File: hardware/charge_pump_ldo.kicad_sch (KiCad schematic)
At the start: 1 part, among them U5 LM27762

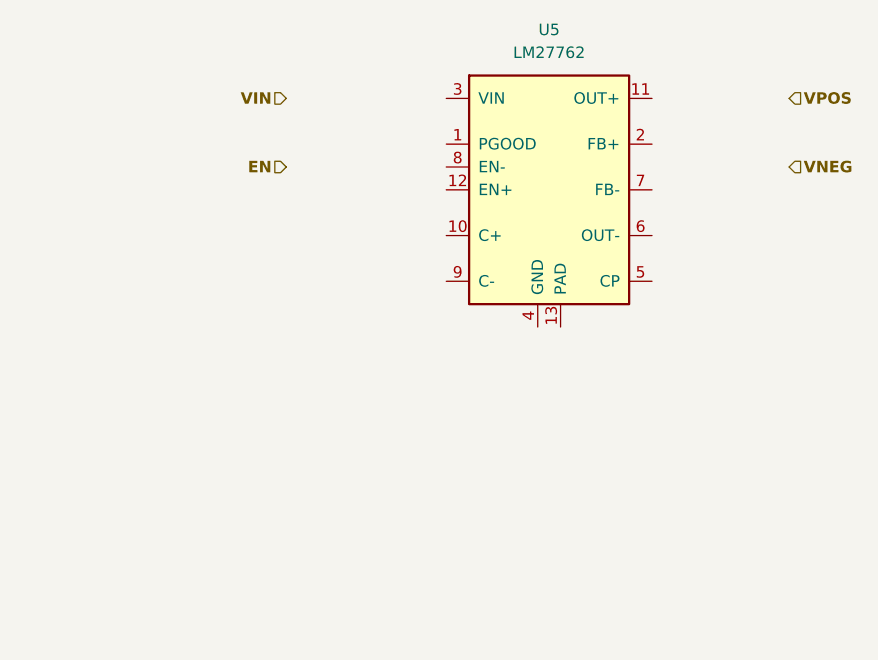
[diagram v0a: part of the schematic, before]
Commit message: Add USB sheet and remove old components
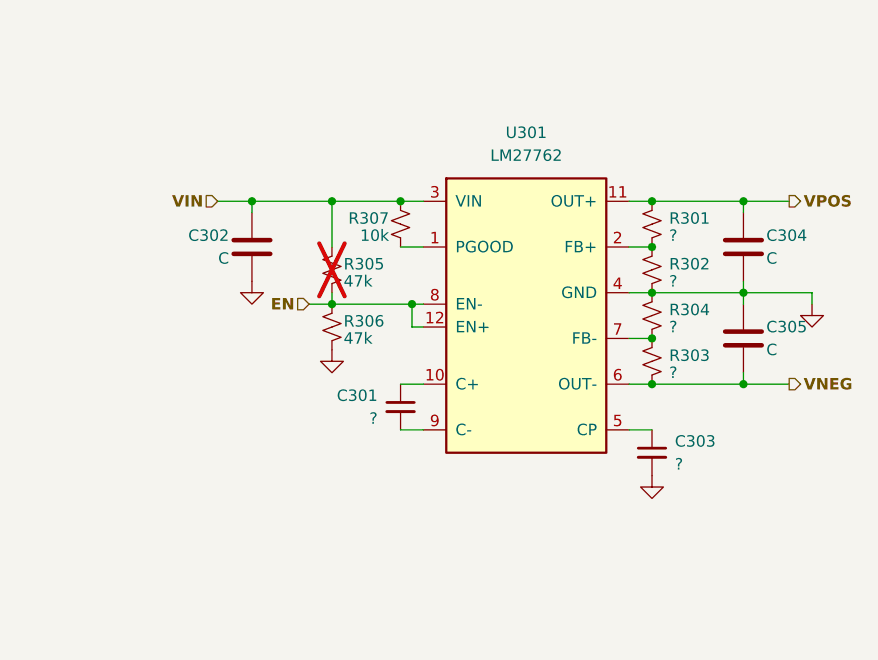
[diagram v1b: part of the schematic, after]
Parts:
- added C301, C303: ?, symbol Device:C_Small
- added C302, C304, C305: C, symbol Device:C
- added R301, R302, R303, R304: ?, symbol Device:R_Small_US
- added R305, R306: 47k, symbol Device:R_Small_US
- added R307: 10k, symbol Device:R_Small_US
- renumbered U5 to U301
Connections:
- net EN: now also U301.12 (EN+), U301.8 (EN-), R305.2, R306.1
- net VIN: now also U301.3 (VIN), C302.1, R305.1, R307.1
- net VNEG: now also U301.6 (OUT-), C305.2, R303.2
- net VPOS: now also U301.11 (OUT+), C304.1, R301.1
- net at U301.1 (PGOOD): now also R307.2
- net at U301.10 (C+): now also C301.1
- net GND: now reaches U301.13 (PAD)
- net GND: now also U301.4 (GND), C302.2, C303.2, C304.2, C305.1, R302.2, R304.1, R306.2
- net at U301.2 (FB+): now also R301.2, R302.1
- net at U301.5 (CP): now also C303.1
- net at U301.7 (FB-): now also R303.1, R304.2
- net at U301.9 (C-): now also C301.2

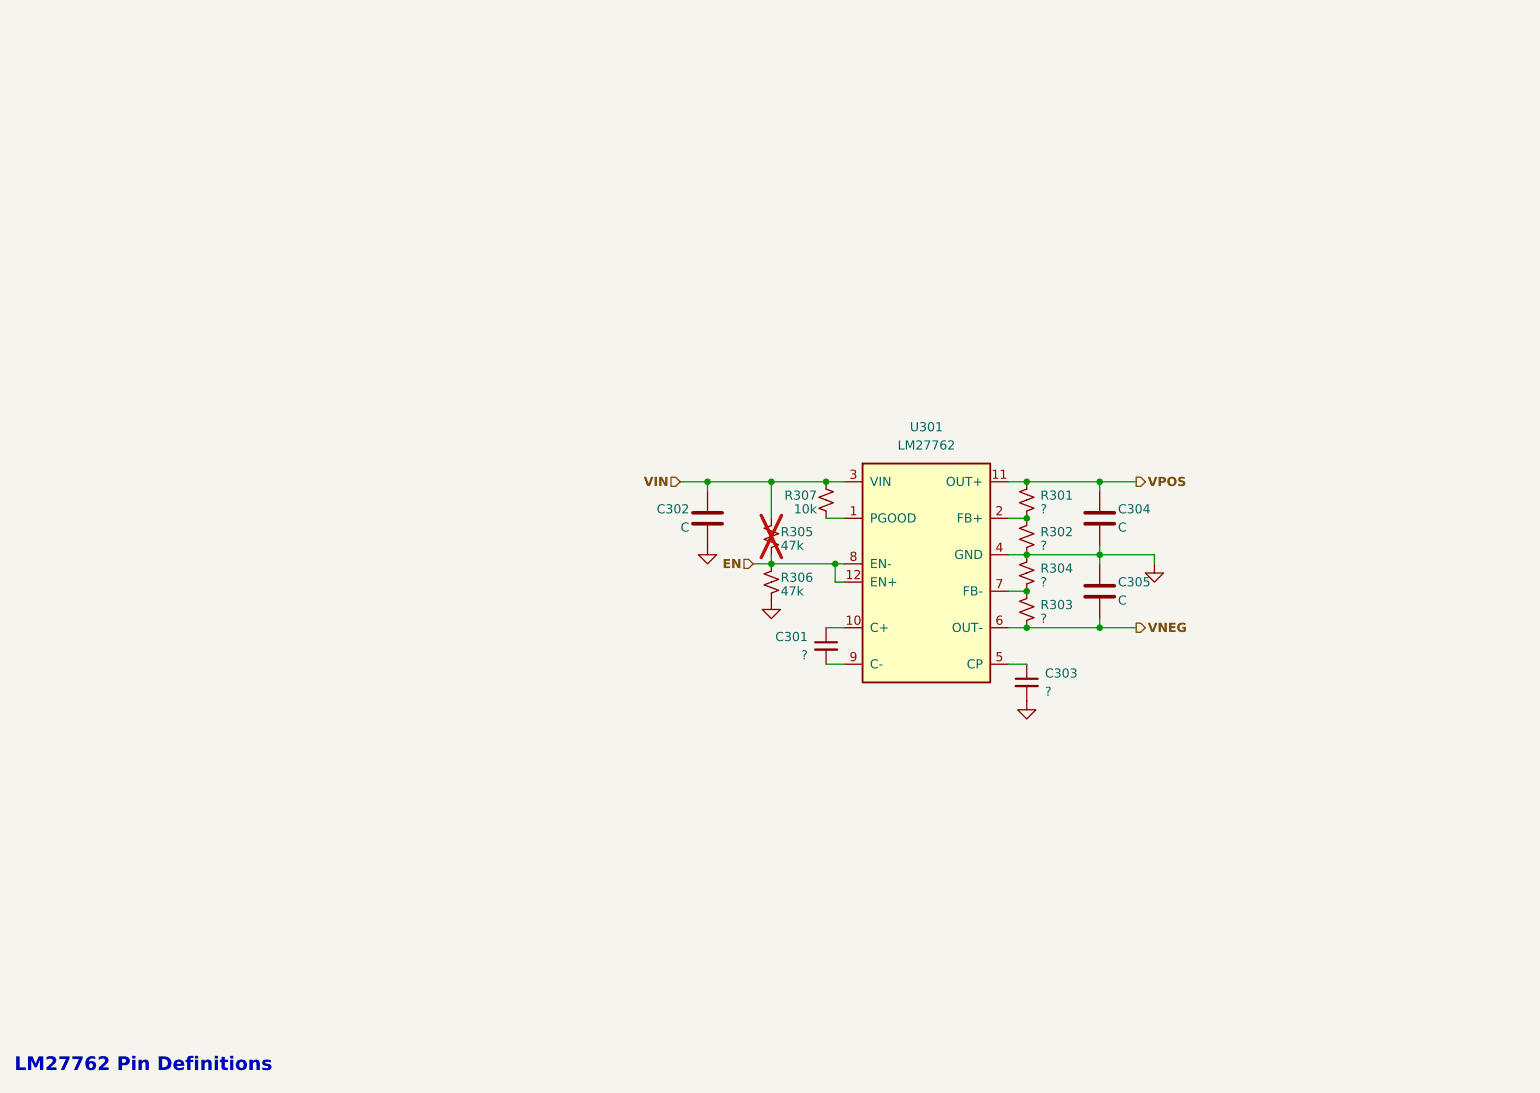
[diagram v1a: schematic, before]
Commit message: Finalize 5V rails
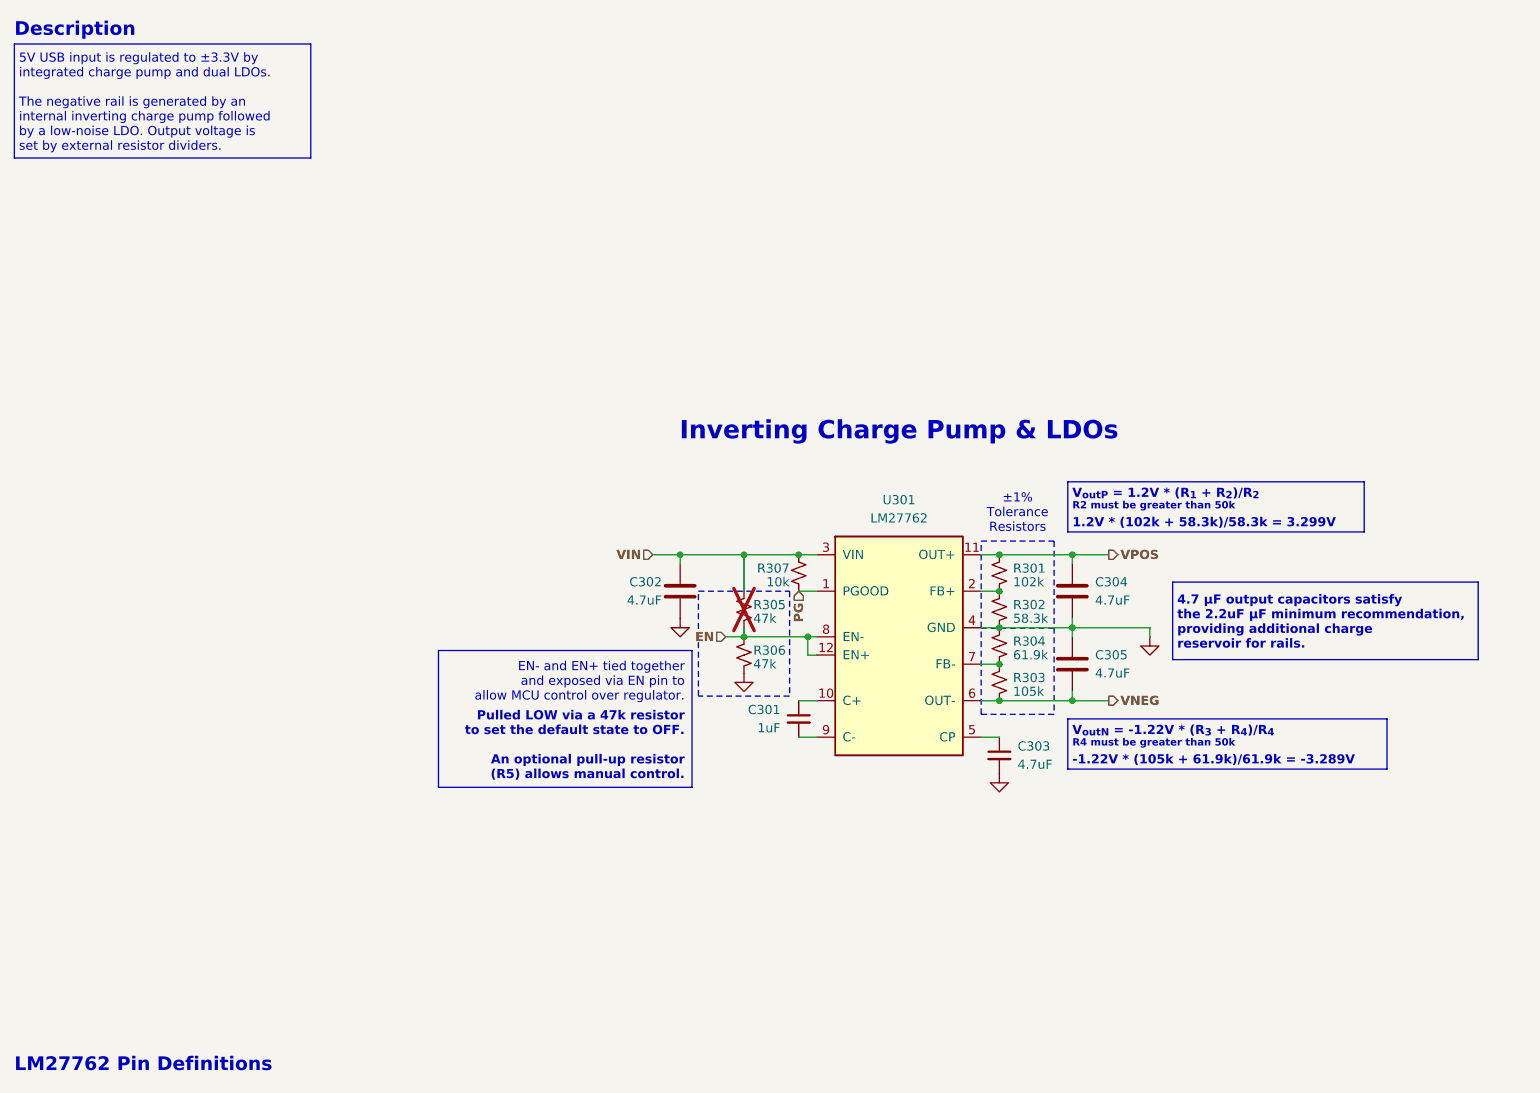
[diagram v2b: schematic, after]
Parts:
- C301: value ? -> 1uF
- C302, C304, C305: value C -> 4.7uF
- C303: value ? -> 4.7uF
- R301: value ? -> 102k; Tolerance (none) -> ±1%
- R302: value ? -> 58.3k; Tolerance (none) -> ±1%
- R303: value ? -> 105k; Tolerance (none) -> ±1%
- R304: value ? -> 61.9k; Tolerance (none) -> ±1%
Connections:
- net PG: now reaches R307.2, U301.1 (PGOOD)
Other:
- note added: "4.7 µF output capacitors satisfy the 2.2uF µF minimum recommendation, providing additional charge reservoir for rails."
- note added: "5V USB input is regulated to ±3.3V by integrated charge pump and dual LDOs. The negative rail is generated by an internal inverting charge pump followed by a low-noise LDO. Output voltage is set by external resistor dividers."
- note added: "Description"
- note added: "EN- and EN+ tied together and exposed via EN pin to allow MCU control over regulator."
- note added: "Inverting Charge Pump & LDOs"
- note added: "Pulled LOW via a 47k resistor to set the default state to OFF. An optional pull-up resistor (R5) allows manual control."
- note added: "V_{outN} = -1.22V * (R_{3} + R_{4})/R_{4} ^{R4 must be greater than 50k} -1.22V * (105k + 61.9k)/61.9k = -3.289V"
- note added: "V_{outP} = 1.2V * (R_{1} + R_{2})/R_{2} ^{R2 must be greater than 50k} 1.2V * (102k + 58.3k)/58.3k = 3.299V"
- note added: "±1% Tolerance Resistors"
- moved on the sheet: C301, C302, C303, C304, C305, R301, R302, R303, R304, R305, R306, R307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

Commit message: Finalize USB interface
Added soft-start
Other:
- title: ±5V Rail Charge Pump & Regulators -> ±3.3V Rail Charge Pump & Regulators
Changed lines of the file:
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@@
 	(paper "A")
 	(title_block
-		(title "±5V Rail Charge Pump & Regulators")
+		(title "±3.3V Rail Charge Pump & Regulators")
 		(rev "A")
 		(company "Jacob Wigent")

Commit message: Finalize power
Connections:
- net VIN renamed VBUS_SW
- net VBUS_SW: no longer R307.1
- net VNEG renamed -3.3VA
- net VPOS renamed +3.3VA
- new net +3.3VD: R307.1
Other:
- note added: "PGOOD exposed with 10k pullup to 3.3VD for MCU monitoring."
- moved on the sheet: R307

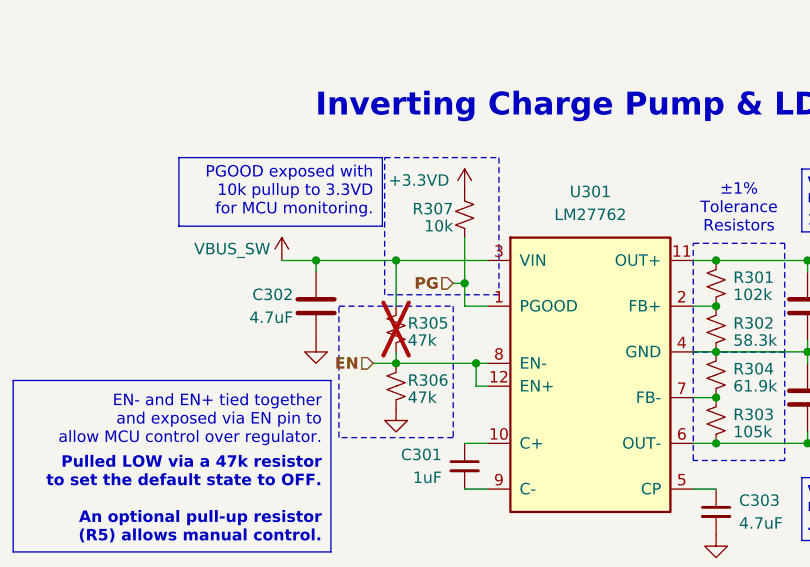
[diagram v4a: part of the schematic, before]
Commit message: Begin MCU pin assignments
Added STM32CubeMX project. Assigned peripheral pins, and began assigning GPIOs.
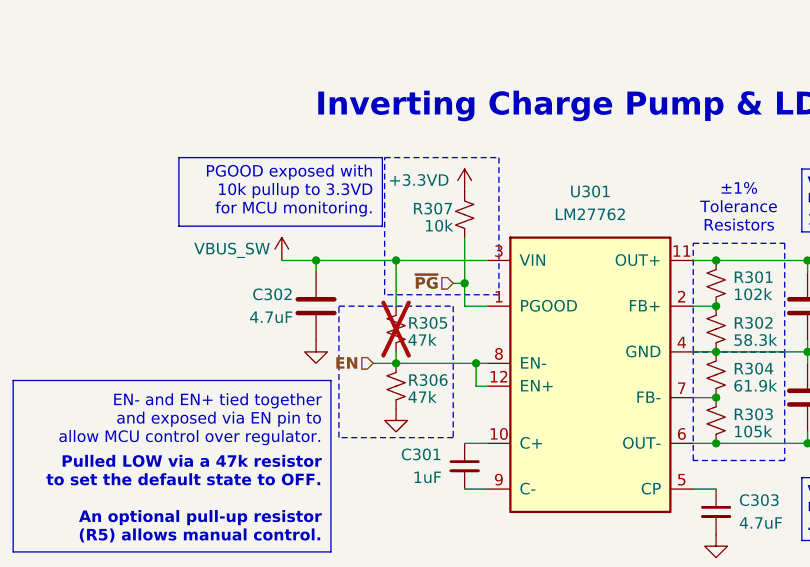
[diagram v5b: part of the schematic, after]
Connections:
- net PG renamed ~{PG}
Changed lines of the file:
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@@
 		)
 	)
-	(hierarchical_label "PG"
+	(hierarchical_label "~{PG}"
 		(shape input)
 		(at 120.65 90.17 180)

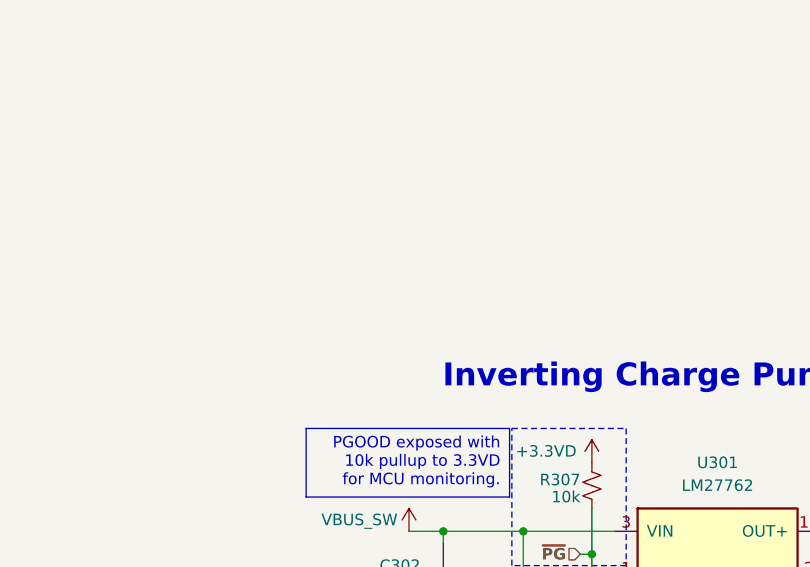
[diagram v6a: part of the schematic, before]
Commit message: Begin VGA impl
Sim and notes on adjusting to 4.5V rails for VGA.
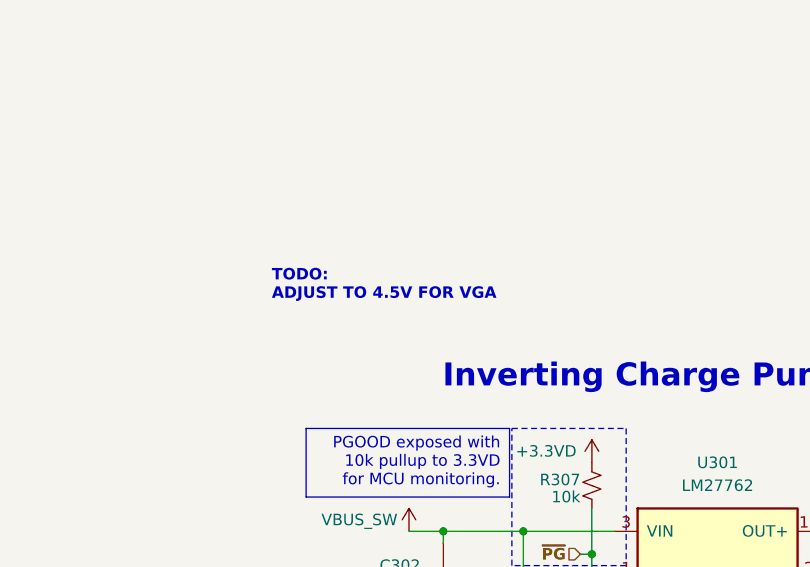
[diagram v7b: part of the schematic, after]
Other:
- note added: "TODO: ADJUST TO 4.5V FOR VGA"
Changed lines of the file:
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@@
+		)
+	)
+	(text "TODO:\nADJUST TO 4.5V FOR VGA"
+		(exclude_from_sim no)
+		(at 86.36 60.325 0)
+		(effects
+			(font
+				(size 1.27 1.27)
+				(thickness 0.254)
+				(bold yes)
+				(color 194 0 0 1)
+			)
+			(justify left)
 		)
 	)

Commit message: Revert VGA selection changes
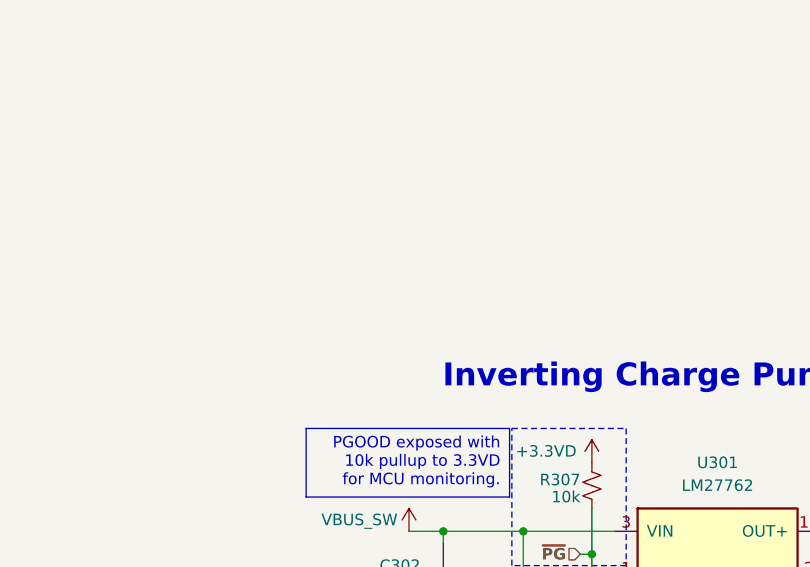
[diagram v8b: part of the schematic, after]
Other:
- note removed: "TODO: ADJUST TO 4.5V FOR VGA"
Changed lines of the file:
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@@
-		)
-	)
-	(text "TODO:\nADJUST TO 4.5V FOR VGA"
-		(exclude_from_sim no)
-		(at 86.36 60.325 0)
-		(effects
-			(font
-				(size 1.27 1.27)
-				(thickness 0.254)
-				(bold yes)
-				(color 194 0 0 1)
-			)
-			(justify left)
 		)
 	)
